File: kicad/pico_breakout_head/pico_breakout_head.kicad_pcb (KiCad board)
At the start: 2 copper layers, 18 parts, among them J1 HDR F 2.54MM 20-pin VERT, J2 HDR F 2.54MM 20-pin VERT, J3 JST B6B-PH-K-S, J4 HDR M 2.54MM 4p VERT, J5 JST B2B-XH-A, J6 HDR M 2.54MM 9p VERT, Q1 BSS123, U1 Pico

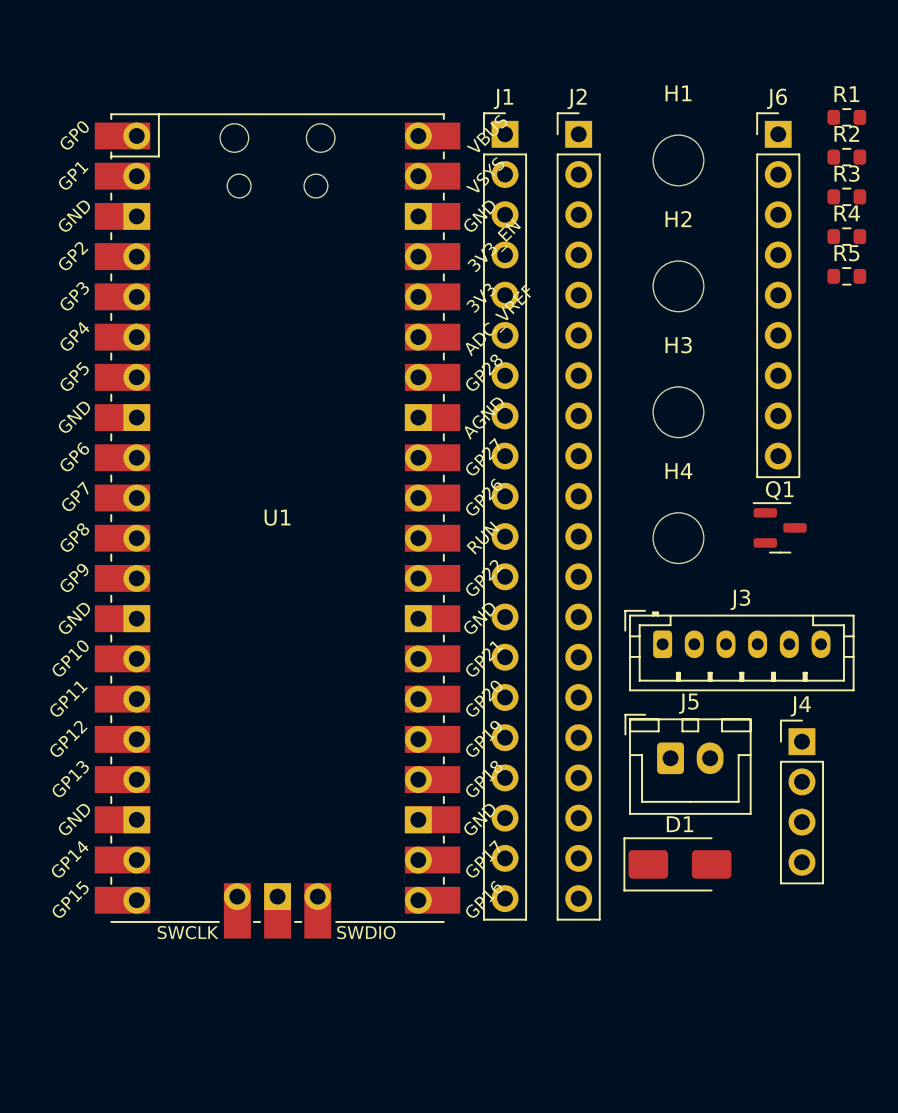
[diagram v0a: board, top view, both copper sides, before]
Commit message: Raspberry Pi Pico head extension PCB proto
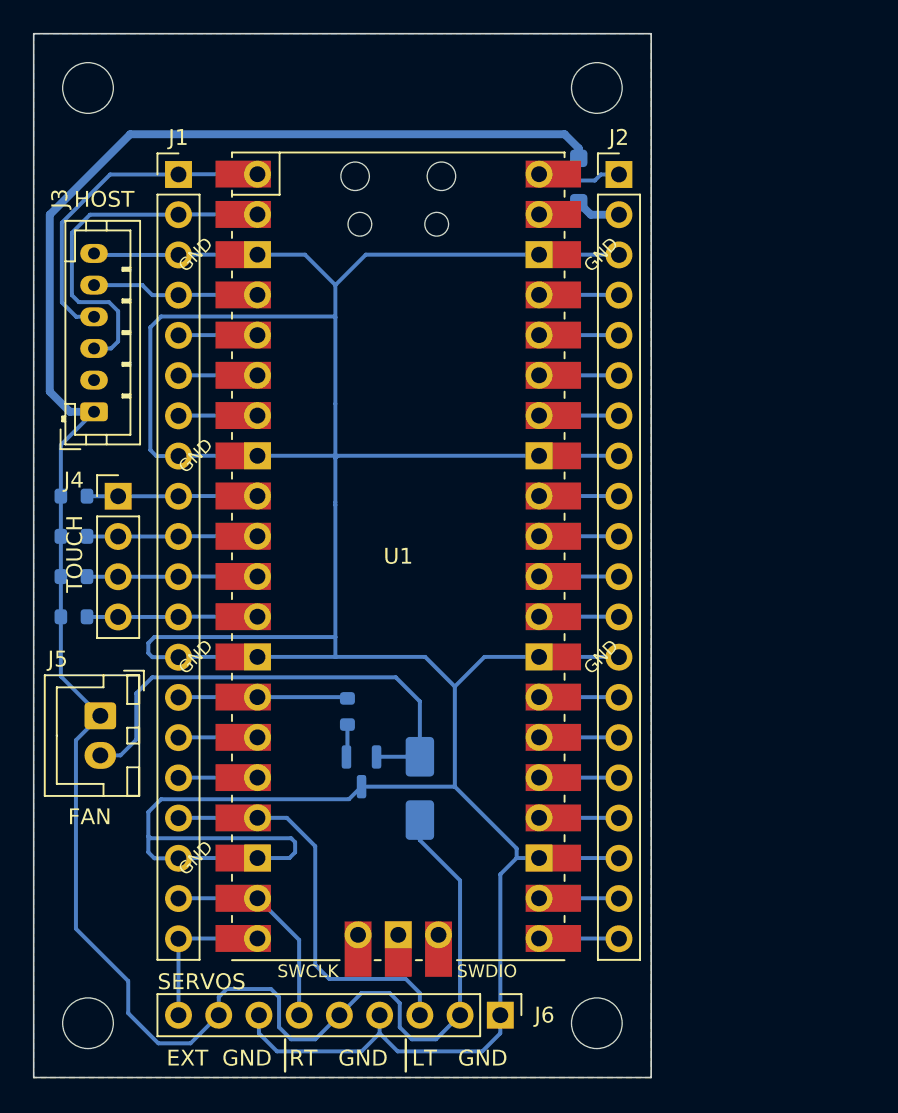
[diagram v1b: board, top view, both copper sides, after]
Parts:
- added D2: FS26, Diode_SMD:D_SOD-123F, B.Cu at (172.7, 73.9)
- D1, Q1, R1, R2, R3, R4, R5: moved to B.Cu
- moved J6 58.3 mm to (167.8, 126.6), turned to -90 degrees
- moved R4 54.4 mm to (140.8, 101.5), turned to 180 degrees
- moved R3 54.4 mm to (140.8, 98.9), turned to 180 degrees
- moved R2 54.4 mm to (140.8, 96.4), turned to 180 degrees
- moved R1 54.3 mm to (140.8, 93.8), turned to 180 degrees
- moved H3 53.7 mm to (141.7, 127.1)
- moved J4 45.9 mm to (143.6, 93.9)
- moved R5 41.8 mm to (158.1, 107.4), turned to 90 degrees
- moved J3 38.8 mm to (142.1, 88.5), turned to 90 degrees
- moved H1 37.6 mm to (141.7, 68.1)
- moved J5 36.1 mm to (142.5, 107.7), turned to -90 degrees
- moved H4 31.1 mm to (173.9, 127.1)
- moved Q1 30.6 mm to (159.0, 111.3), turned to -90 degrees
- moved J1 20.8 mm to (147.4, 73.5)
- moved D1 17.1 mm to (162.7, 112.3), turned to 90 degrees
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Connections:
- net /I2C_SCL_MASTER renamed /I2C_SCL_HOST
- net /I2C_SDA_MASTER renamed /I2C_SDA_HOST
- net /INT_MASTER renamed /INT_HOST
- J1 pad 13: +5V -> GND
- J1 pad 17: Net-(J1-Pin_17) -> /SERVO_LEFT
- J1 pad 18: +5V -> GND
- J1 pad 19: Net-(J1-Pin_19) -> /SERVO_RIGHT
- J1 pad 20: Net-(J1-Pin_20) -> /SERVO_EXT
- J1 pad 3: +5V -> GND
- J1 pad 5: /SERVO_LEFT -> Net-(J1-Pin_5)
- J1 pad 6: /SERVO_RIGHT -> Net-(J1-Pin_6)
- J1 pad 7: /SERVO_EXT -> Net-(J1-Pin_7)
- J1 pad 8: +5V -> GND
- J2 pad 13: +5V -> GND
- J2 pad 18: +5V -> GND
- J2 pad 3: +5V -> GND
- J2 pad 8: +5V -> GND
- J3 pad 6: +5V -> GND
- J6 pad 1: +5V -> GND
- J6 pad 4: +5V -> GND
- J6 pad 7: +5V -> GND
- Q1 pad 3: +5V -> GND
- U1 pad 13: +5V -> GND
- U1 pad 17: Net-(J1-Pin_17) -> /SERVO_LEFT
- U1 pad 18: +5V -> GND
- U1 pad 19: Net-(J1-Pin_19) -> /SERVO_RIGHT
- U1 pad 20: Net-(J1-Pin_20) -> /SERVO_EXT
- U1 pad 23: +5V -> GND
- U1 pad 28: +5V -> GND
- U1 pad 3: +5V -> GND
- U1 pad 33: +5V -> GND
- U1 pad 38: +5V -> GND
- U1 pad 5: /SERVO_LEFT -> Net-(J1-Pin_5)
- U1 pad 6: /SERVO_RIGHT -> Net-(J1-Pin_6)
- U1 pad 7: /SERVO_EXT -> Net-(J1-Pin_7)
- U1 pad 8: +5V -> GND
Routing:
- net GND: track 0.00 -> 243.9 mm
- net +5V: track 0.00 -> 136.5 mm
- net Net-(D1-A): track 0.00 -> 30.8 mm
- net /SERVO_LEFT: track 0.00 -> 25.6 mm
- net /I2C_SCL_HOST: track 0.00 -> 23.1 mm
- net /I2C_SDA_HOST: track 0.00 -> 21.1 mm
- net /SERVO_RIGHT: track 0.00 -> 13.5 mm
- net /TOUCH_RIGHT: track 0.00 -> 10.8 mm
- net /TOUCH_REAR: track 0.00 -> 10.8 mm
- net /TOUCH_LEFT: track 0.00 -> 10.8 mm
- net /TOUCH_TOP: track 0.00 -> 10.8 mm
- net /FAN_EN: track 0.00 -> 10.7 mm
- net /INT_HOST: track 0.00 -> 10.6 mm
- net /SERVO_EXT: track 0.00 -> 9.82 mm
- net Net-(D2-K): track 0.00 -> 5.67 mm
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- added copper zone on B.Cu, net GND
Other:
- board outline added: 39 x 65.9 mm
- board text added: "EXT GND"
- board text added: "FAN"
- board text added: "HOST"
- board text added: "LT GND"
- board text added: "RT GND"
- board text added: "SERVOS"
- board text added: "TOUCH"

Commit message: KiCAD bugfix?
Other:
- board size 39 x 65.9 mm -> 39 x 66 mm
- board text added: "Pico Head Breakout PCB v0.1 makerspet.com"
- board text added: "makerspet.com"
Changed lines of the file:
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@@
     (property "ki_keywords" "connector")
     (attr through_hole)
-    (fp_text reference "J2" (at 0 -2.33) (layer "F.SilkS")
+    (fp_text reference "J2" (at 0 -2.413) (layer "F.SilkS")
         (effects (font (size 1 1) (thickness 0.15)))
     )
@@
         (effects (font (size 1 1) (thickness 0.15)))
     )
-    (fp_text user "${REFERENCE}" (at 0 24.13 90) (layer "F.Fab")
+    (fp_text user "${REFERENCE}" (at 0 -2.413 180) (layer "F.Fab")
         (effects (font (size 1 1) (thickness 0.15)))
     )
@@
         (effects (font (size 0.8 0.8) (thickness 0.15)) (justify mirror))
     )
+    (fp_text user "GND" (at 6.696 6.35 -45) (layer "B.SilkS")
+        (effects (font (size 0.8 0.8) (thickness 0.15)) (justify mirror))
+    )
     (fp_text user "ADC_VREF" (at 5.496 -12.61 -45) (layer "B.SilkS")
         (effects (font (size 0.8 0.8) (thickness 0.15)) (justify mirror))
     )
+    (fp_text user "GND" (at 6.696 19.05 -45) (layer "B.SilkS")
+        (effects (font (size 0.8 0.8) (thickness 0.15)) (justify mirror))
+    )
     (fp_text user "GP21" (at 6.442 8.79 -45) (layer "B.SilkS")
         (effects (font (size 0.8 0.8) (thickness 0.15)) (justify mirror))
@@
         (effects (font (size 0.8 0.8) (thickness 0.15)) (justify mirror))
     )
+    (fp_text user "GND" (at -6.766 -19.05 315) (layer "B.SilkS")
+        (effects (font (size 0.8 0.8) (thickness 0.15)) (justify mirror))
+    )
     (fp_text user "GP20" (at 6.442 11.32 -45) (layer "B.SilkS")
         (effects (font (size 0.8 0.8) (thickness 0.15)) (justify mirror))
@@
         (effects (font (size 0.8 0.8) (thickness 0.15)) (justify mirror))
     )
+    (fp_text user "GND" (at -6.766 -6.35 315) (layer "B.SilkS")
+        (effects (font (size 0.8 0.8) (thickness 0.15)) (justify mirror))
+    )
     (fp_text user "GP4" (at -6.766 -11.43 -45) (layer "B.SilkS")
         (effects (font (size 0.8 0.8) (thickness 0.15)) (justify mirror))
@@
         (effects (font (size 0.8 0.8) (thickness 0.15)) (justify mirror))
     )
+    (fp_text user "GND" (at 6.696 -19.05 -45) (layer "B.SilkS")
+        (effects (font (size 0.8 0.8) (thickness 0.15)) (justify mirror))
+    )
     (fp_text user "GP13" (at -6.512 16.51 -45) (layer "B.SilkS")
         (effects (font (size 0.8 0.8) (thickness 0.15)) (justify mirror))
@@
         (effects (font (size 0.8 0.8) (thickness 0.15)) (justify mirror))
     )
-    (fp_text user "GND" (at 12.8 6.35 45) (layer "F.SilkS")
-        (effects (font (size 0.8 0.8) (thickness 0.15)))
-    )
-    (fp_text user "GND" (at -12.8 19.05 45) (layer "F.SilkS")
-        (effects (font (size 0.8 0.8) (thickness 0.15)))
-    )
-    (fp_text user "GND" (at -12.8 -19.05 45) (layer "F.SilkS")
-        (effects (font (size 0.8 0.8) (thickness 0.15)))
+    (fp_text user "GND" (at -6.639 6.35 -45) (layer "B.SilkS")
+        (effects (font (size 0.8 0.8) (thickness 0.15)) (justify mirror))
     )
     (fp_text user "SWCLK" (at -5.7 26.2) (layer "F.SilkS")
@@
     (fp_text user "SWDIO" (at 5.6 26.2) (layer "F.SilkS")
         (effects (font (size 0.8 0.8) (thickness 0.15)))
-    )
-    (fp_text user "GND" (at -12.8 -6.35 45) (layer "F.SilkS")
-        (effects (font (size 0.8 0.8) (thickness 0.15)))
-    )
-    (fp_text user "GND" (at 12.8 -19.05 45) (layer "F.SilkS")
-        (effects (font (size 0.8 0.8) (thickness 0.15)))
-    )
-    (fp_text user "GND" (at -12.8 6.35 45) (layer "F.SilkS")
-        (effects (font (size 0.8 0.8) (thickness 0.15)))
-    )
-    (fp_text user "Copper Keepouts shown on Dwgs layer" (at 0.1 -30.2) (layer "Cmts.User")
-        (effects (font (size 1 1) (thickness 0.15)))
     )
     (fp_text user "${REFERENCE}" (at 0 0 180) (layer "F.Fab")
@@
     (property "ki_keywords" "connector")
     (attr through_hole)
-    (fp_text reference "J1" (at 0 -2.33) (layer "F.SilkS")
+    (fp_text reference "J1" (at 0 -2.413) (layer "F.SilkS")
         (effects (font (size 1 1) (thickness 0.15)))
     )
@@
         (effects (font (size 1 1) (thickness 0.15)))
     )
-    (fp_text user "${REFERENCE}" (at 0 24.13 90) (layer "F.Fab")
+    (fp_text user "${REFERENCE}" (at 0 -2.413) (layer "F.Fab")
         (effects (font (size 1 1) (thickness 0.15)))
     )
@@
     (property "ki_keywords" "connector")
     (attr through_hole)
-    (fp_text reference "J4" (at -2.794 -1.016 180) (layer "F.SilkS")
+    (fp_text reference "J4" (at -2.794 -0.889 180) (layer "F.SilkS")
         (effects (font (size 1 1) (thickness 0.15)))
     )
@@
         (effects (font (size 1 1) (thickness 0.15)))
     )
-    (fp_text user "${REFERENCE}" (at 0 3.81 90) (layer "F.Fab")
+    (fp_text user "${REFERENCE}" (at -2.794 -0.889 180) (layer "F.Fab")
         (effects (font (size 1 1) (thickness 0.15)))
     )
@@
     )
   )
+  (gr_line (start 156.8115 72.5) (end 156.8115 77.724)
+    (stroke (width 0.15) (type default)) (layer "F.SilkS"))
+  (gr_line (start 156.8115 77.724) (end 165.8335 77.724)
+    (stroke (width 0.15) (type default)) (layer "F.SilkS"))
   (gr_line (start 154.178 128.143) (end 154.178 130.175)
     (stroke (width 0.15) (type default)) (layer "F.SilkS"))
   (gr_line (start 161.798 128.143) (end 161.798 130.175)
     (stroke (width 0.15) (type default)) (layer "F.SilkS"))
-  (gr_rect (start 138.303 64.643) (end 177.292 130.556)
+  (gr_line (start 165.8335 77.724) (end 165.8335 72.5)
+    (stroke (width 0.15) (type default)) (layer "F.SilkS"))
+  (gr_rect (start 138.303 64.643) (end 177.303 130.643)
     (stroke (width 0.1) (type default)) (fill none) (layer "Edge.Cuts"))
+  (gr_text "makerspet.com" (at 160.655 102.743 -90) (layer "B.SilkS")
+    (effects (font (size 1 1) (thickness 0.15)) (justify left bottom mirror))
+  )
   (gr_text "LT   GND" (at 162.179 129.921) (layer "F.SilkS")
     (effects (font (size 1 1) (thickness 0.15)) (justify left bottom))
+  )
+  (gr_text "Pico Head Breakout PCB v0.1\nmakerspet.com" (at 157.803 68.4784) (layer "F.SilkS")
+    (effects (font (size 1 1) (thickness 0.15)) (justify bottom))
   )
   (gr_text "EXT  GND" (at 146.685 129.921) (layer "F.SilkS")
@@
     (polygon
       (pts
-        (xy 138.303 64.643)
-        (xy 177.292 64.643)
-        (xy 177.292 130.556)
-        (xy 138.303 130.556)
+        (xy 138.176 64.516)
+        (xy 177.419 64.516)
+        (xy 177.419 130.81)
+        (xy 138.176 130.81)
       )
     )

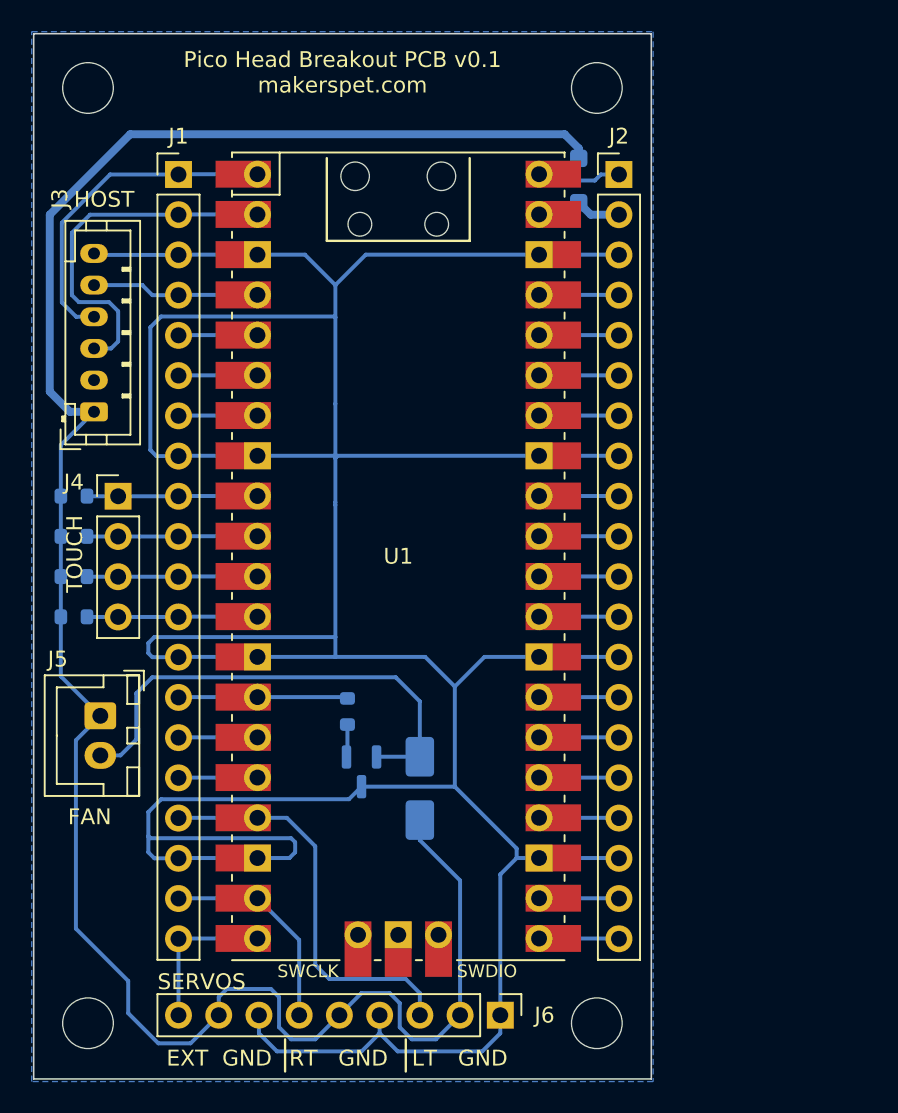
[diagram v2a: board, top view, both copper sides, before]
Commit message: Socket header
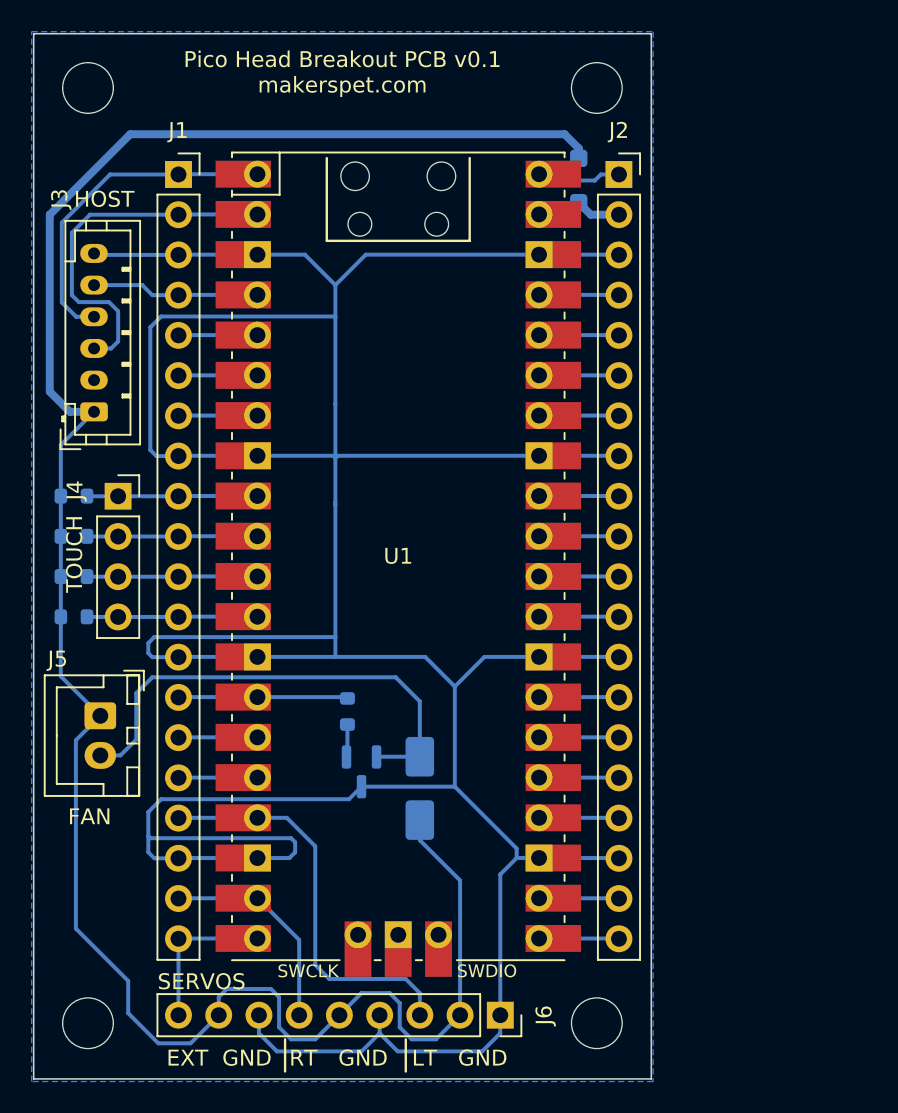
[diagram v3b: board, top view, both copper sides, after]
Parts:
- J1, J2: footprint Connector_PinHeader_2.54mm:PinHeader_1x20_P2.54mm_Vertical -> Connector_PinSocket_2.54mm:PinSocket_1x20_P2.54mm_Vertical
- J4: footprint Connector_PinHeader_2.54mm:PinHeader_1x04_P2.54mm_Vertical -> Connector_PinSocket_2.54mm:PinSocket_1x04_P2.54mm_Vertical
- J6: footprint Connector_PinHeader_2.54mm:PinHeader_1x09_P2.54mm_Vertical -> Connector_PinSocket_2.54mm:PinSocket_1x09_P2.54mm_Vertical

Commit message: Pico head PCB 0.1.1
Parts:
- removed R5: 1k, Resistor_SMD:R_0603_1608Metric
- D1: value CGRA4004-G -> FS26; footprint Diode_SMD:D_SMA -> Diode_SMD:D_SOD-123F
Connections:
- Q1 pad 1: Net-(Q1-G) -> /FAN_EN
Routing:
- net /FAN_EN: track 10.7 -> 14.4 mm
- net Net-(Q1-G): track 2.07 -> 0.00 mm
- net Net-(D1-A): track 30.8 -> 31.6 mm
- net +5V: track 136.5 -> 137.1 mm
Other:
- board text added: "Pico Head Breakout PCB v0.1.1 makerspet.com"
- board text removed: "Pico Head Breakout PCB v0.1 makerspet.com"
